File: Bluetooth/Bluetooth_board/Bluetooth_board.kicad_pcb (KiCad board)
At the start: 2 copper layers, 29.9 x 21.2 mm, 5 parts, among them J10 PINHD_1x2_Male, J11 PINHD_1x2_Male, J2 PINHD_1x6_Female, J6 PINHD_1x2_Male, U5 BM64SPKS1MC2-0003AA

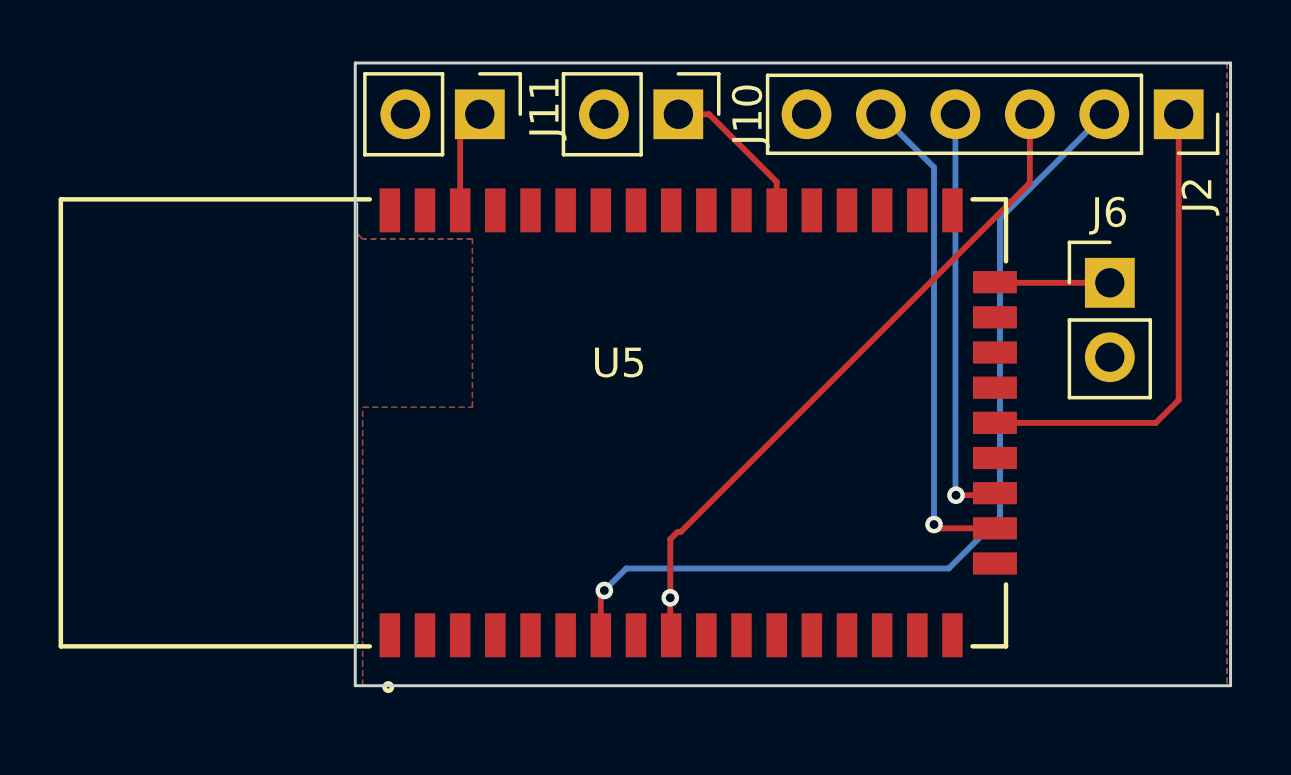
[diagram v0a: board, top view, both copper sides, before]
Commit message: SMD5 + carrier: solder jumpers, C10/C11 to a disc footprint, 2-pin programming header
- SMD5: JP2/JP3 solder jumpers placed; C10/C11 100 uF 1206 -> 47 uF on
  Capacitor_THT:C_Disc_D4.7mm_W2.5mm_P5.00mm (DNP, fit 1 uF to use J7)
- Carrier: programming header down to 2 pins (P2_0, RST_N) now that MFB
  reaches the module through the main 8-pin link -- this also removes the
  hazard of MFB being driven from two connectors at once
- Cross-reference fixes missed by the hardware-doc split commit
- .gitignore: the Bluetooth carrier lives outside hardware/kicad/, so repeat
  the jlcpcb/, production_files/, tmp*.rpt and _restore_backup_* rules there

KNOWN ISSUE, not fixed here: carrier J1 pins 2 and 3 are swapped, so ESP TX
meets BM64 TX and ESP RX meets BM64 RX. See the next commit.

Co-Authored-By: Claude Opus 5 <noreply@anthropic.com>
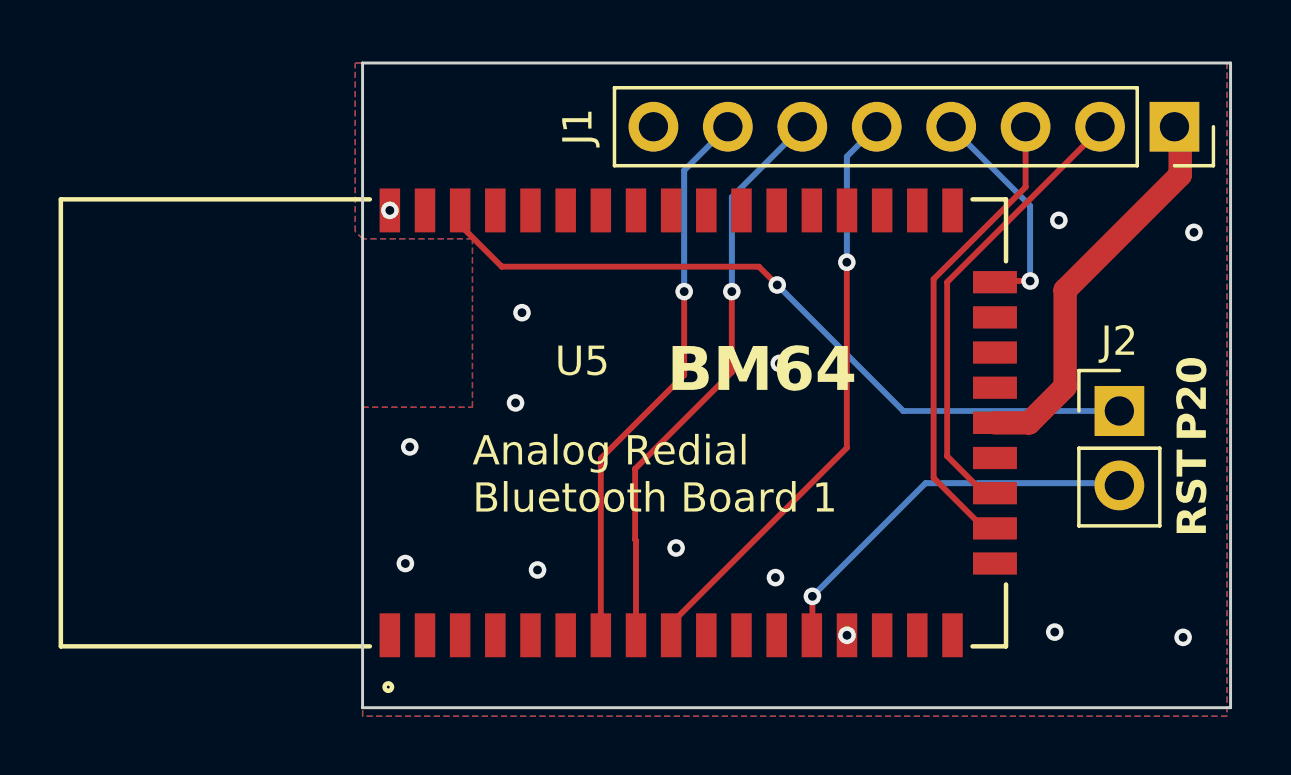
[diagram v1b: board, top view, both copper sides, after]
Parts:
- removed J10, J11, J6: PINHD_1x2_Male, Connector_PinHeader_2.54mm:PinHeader_1x02_P2.54mm_Vertical
- added J1: PINHD_1x8_Female, Connector_PinSocket_2.54mm:PinSocket_1x08_P2.54mm_Vertical, F.Cu at (150.2, 77.2)
- J2: value PINHD_1x6_Female -> PINHD_1x4_Male; footprint Connector_PinSocket_2.54mm:PinSocket_1x06_P2.54mm_Vertical -> Connector_PinHeader_2.54mm:PinHeader_1x02_P2.54mm_Vertical
- moved J2 10.3 mm to (148.3, 86.9), turned to 0 degrees
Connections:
- J2 pad 1: +3.3V -> Net-(U5-P2_0)
- J2 pad 2: /A0HPL -> /RST
- U5 pad 13: unconnected-(U5-RST_N-Pad13) -> /RST
- U5 pad 32: Net-(U5-EAN) -> unconnected-(U5-EAN-Pad32)
- U5 pad 8: unconnected-(U5-MIC_N1-Pad8) -> /Mic_N1
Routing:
- net Net-(U5-P2_0): track 3.56 -> 25.6 mm, vias 0 -> 1
- net /Mic_N1: track 0.00 -> 19.7 mm, vias 0 -> 1
- net /RST: track 0.00 -> 13.4 mm, vias 0 -> 1
- net /A0HPL: track 31.3 -> 19.2 mm
- net Net-(U5-EAN): track 5.28 -> 0.00 mm
- net Net-(U5-MFB): track 3.93 -> 7.60 mm, vias 0 -> 1
- net +3.3V: track 16.3 -> 13.5 mm
- net /Mic_P1: track 22.9 -> 20.3 mm
- net /espUartRx: track 14.4 -> 15.6 mm, vias 1 -> 0
- net /espUartTx: track 16.9 -> 16.1 mm, vias 1 -> 0
- net GND: vias 0 -> 14
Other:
- board size 29.9 x 21.2 mm -> 29.6 x 22 mm
- board text added: "Analog Redial Bluetooth Board 1"
- board text added: "BM64"
- board text added: "P20"
- board text added: "RST"
